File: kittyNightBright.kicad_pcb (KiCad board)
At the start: 2 copper layers, 53.6 x 68.3 mm, 9 parts, among them Q1 NPN, SW1 SW_Push

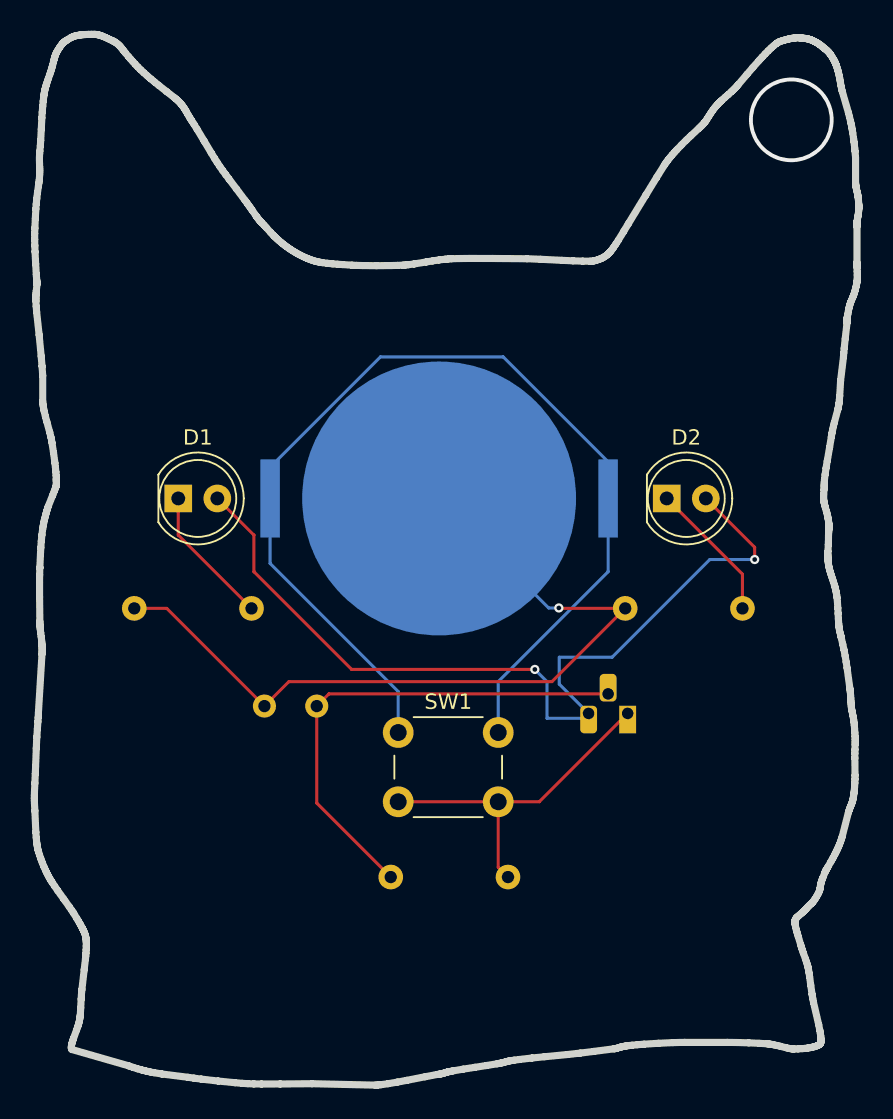
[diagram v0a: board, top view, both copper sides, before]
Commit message: fixed silkscreen
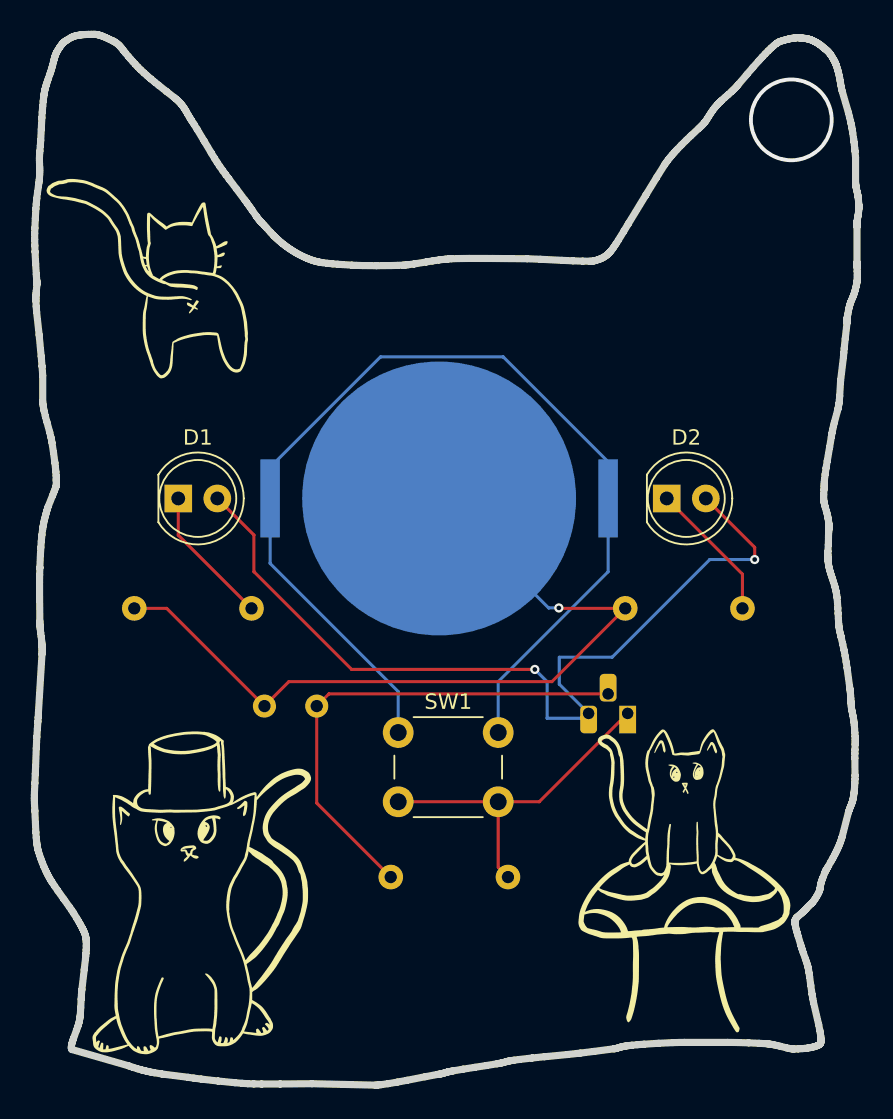
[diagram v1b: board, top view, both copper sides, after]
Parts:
- added G***: LOGO, LOGO, F.Cu at (178.6, 124.6)
- added G***: LOGO, LOGO, F.Cu at (146.1, 86.5)
- added G***: LOGO, LOGO, F.Cu at (147.6, 124.6)
